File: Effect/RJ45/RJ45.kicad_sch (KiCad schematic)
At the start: 6 parts, among them J1 Conn_01x04_Pin, J2 RJ45, J3 Conn_01x03_Pin

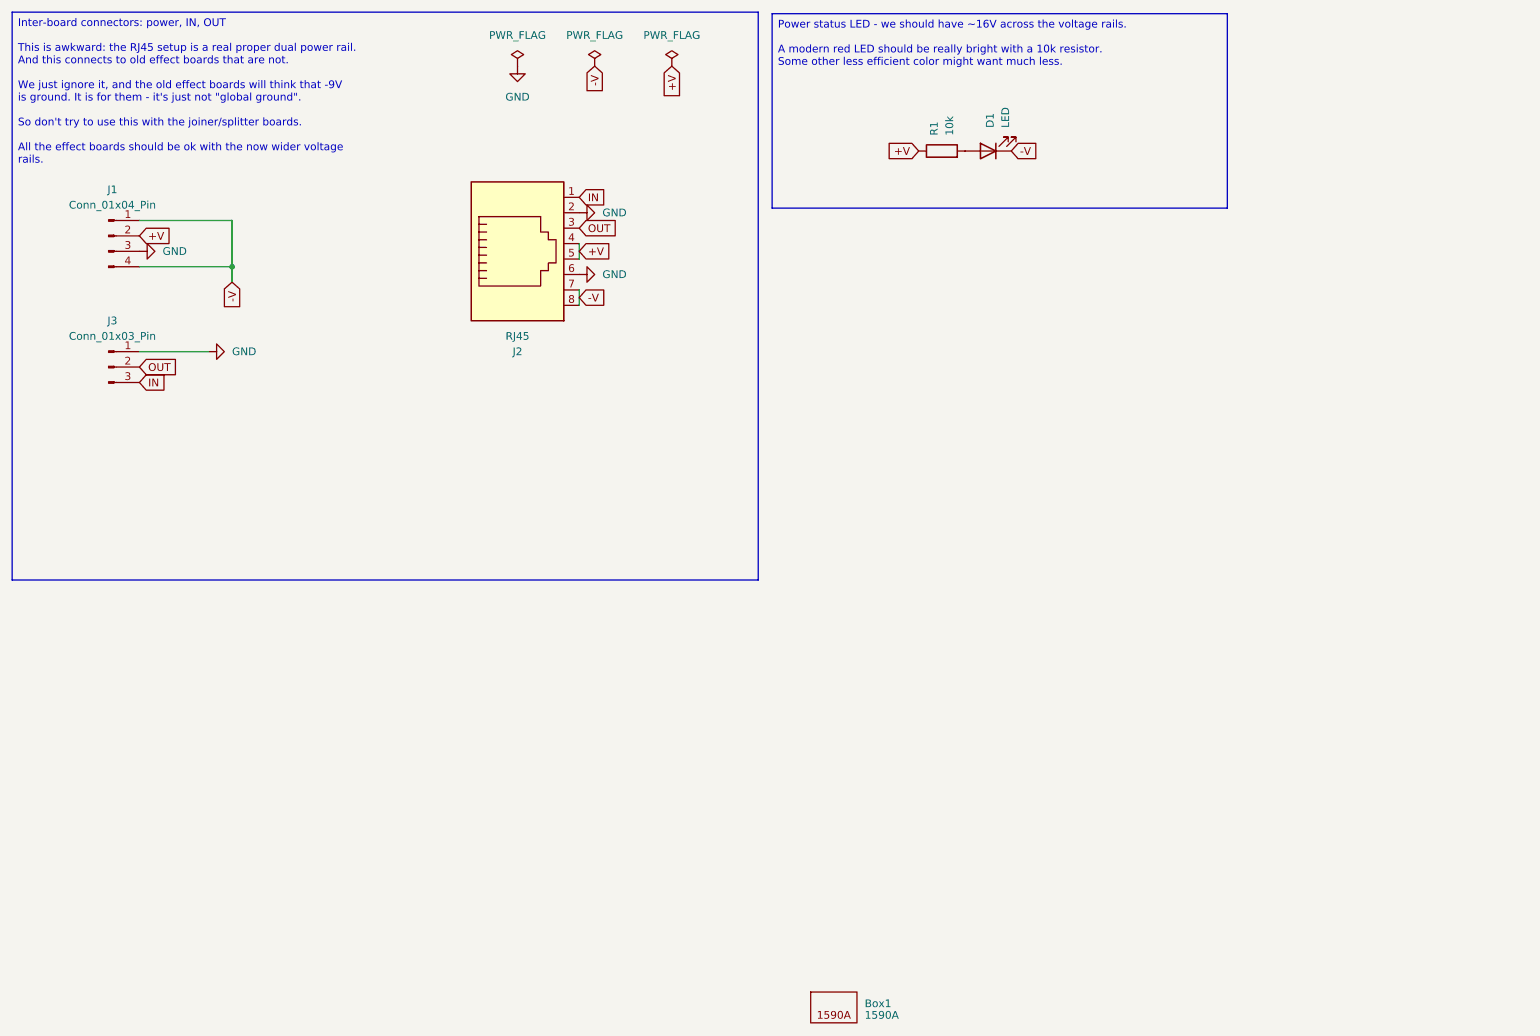
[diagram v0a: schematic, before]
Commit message: Switch to a shielded RJ45 connector for the RJ45 test boards
It turns out that all my ethernet cables I had around look to be plain
unshielded twisted pairs (UTP), and some very preliminary testing shows
that they are very noisy and I'd need to use differential signalling to
make the whole "connect the base and effect with an ethernet cable"
scheme work.

I know, I know, that's technically the right thing to do anyway, but I
really don't think it's an option.  It adds way too much effort at the
effects end, at that point I'm better off just keeping the two together.

Even if some of my recent circuits have been differential (ie that whole
multiplier thing), I don't want to force that on everything.

And yes, the ethernet cable idea might have been a stupid idea and any
first-year EE would probably have told me that.  I'm a SW guy, remember?

But before giving up, let's just try the single-ended model with proper
shielded cables and shielded connectors.  The double-shielded cables are
a thing, with each twisted pair foil-shielded and then the whole cable
having a braided shield.

That would seem to be no worse than a normal 1/4" audio cable, even if
the same cable also carries power.  I'm looking for a few feet, not long
runs.  Knock wood.

And the shielding is part of the CAT8 specs, so this is standard cable
these days and cheap, even if my random box of cables was full of the
old crappy stuff of yesteryear.

So maybe this model is still salvageable with single-ended signaling.
Because I'd love to separate the stomp switch and audio jacks from the
actual effect side.

Signed-off-by: Linus Torvalds <torvalds@linux-foundation.org>
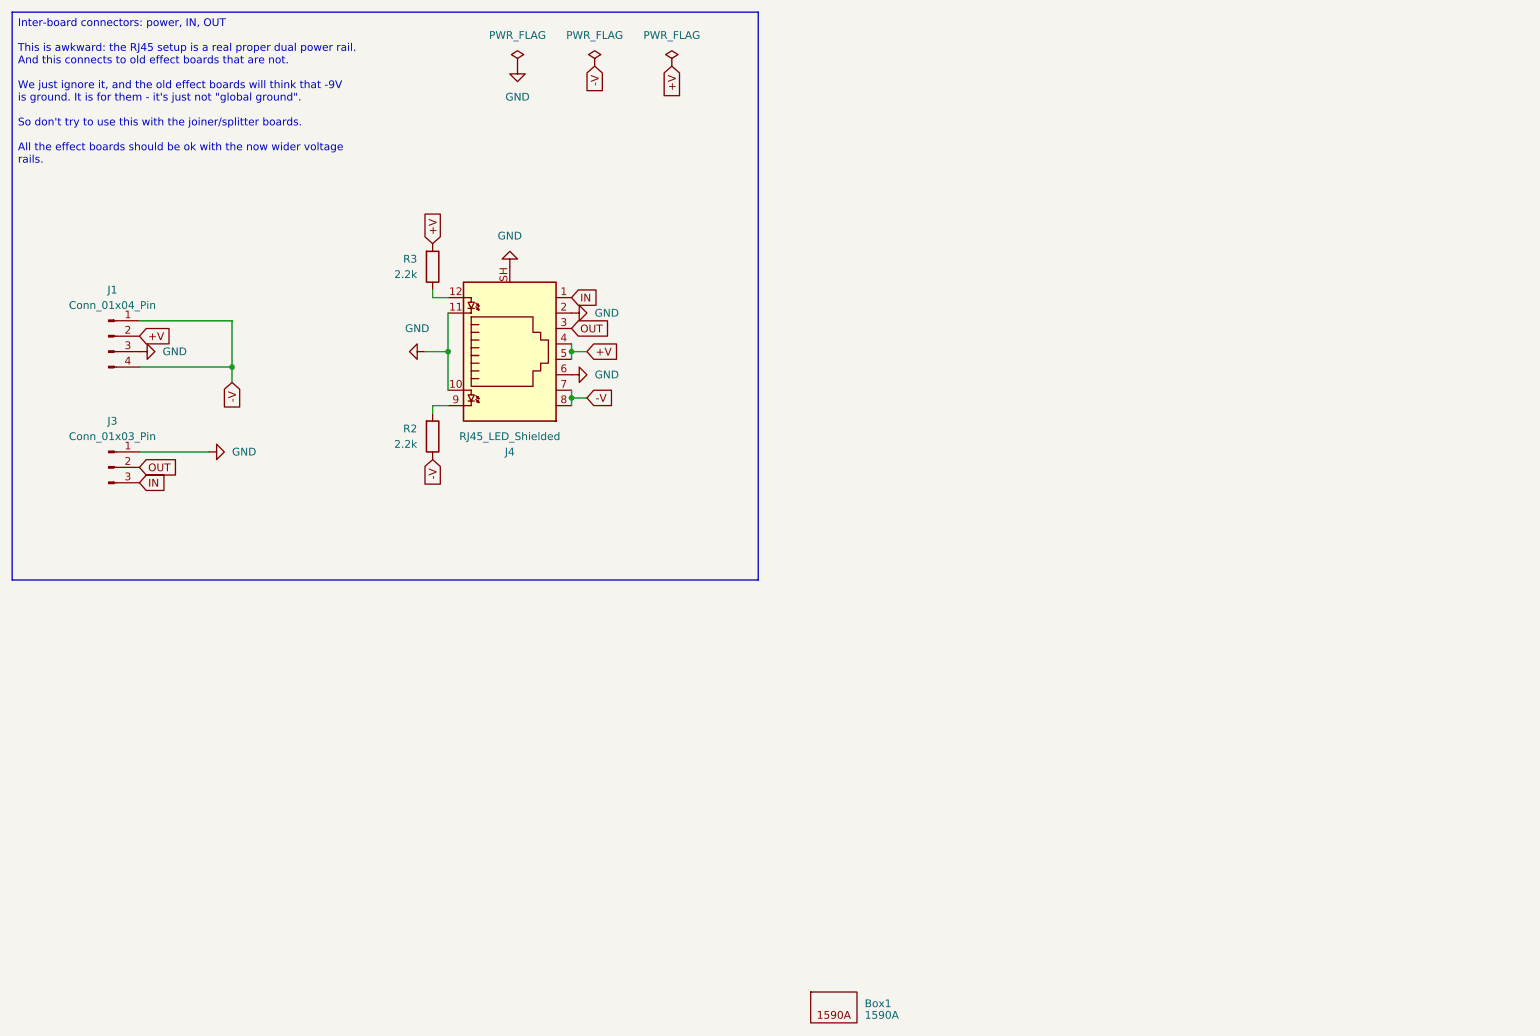
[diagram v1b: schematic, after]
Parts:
- removed D1: LED, Mylib:Würth Reverse Mount LED, symbol Device:LED
- removed J2: RJ45, Connector_RJ:RJ45_OST_PJ012-8P8CX_Vertical, symbol Connector:RJ45
- removed R1: 10k, Resistor_SMD:R_0805_2012Metric, symbol Device:R
- added J4: RJ45_LED_Shielded, Connector_RJ:RJ45_Amphenol_RJHSE538X, symbol Connector:RJ45_LED_Shielded
- added R2, R3: 2.2k, Resistor_SMD:R_0805_2012Metric, symbol Device:R
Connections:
- net +V: now also J4.4, J4.5, R3.2
- net -V: now also J4.7, J4.8, R2.1
- net GND: now also J4.10, J4.11, J4.2, J4.6, J4.SH
- net IN: now also J4.1
- net OUT: now also J4.3
- new net: J4.12, R3.1
- new net: J4.9, R2.2
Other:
- moved on the sheet: J1, J3

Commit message: RJ45: update the "effect conversion" board to be active
... and hopefully make it work right.

The old hacky one was truly just a hack, and was a passive feed-through
of the signals from the RJ45 jack to the old effect board pin headers.

That was hacky mainly because it ignored the whole new world order wrt
voltages (ie the RJ45 cable carries dual voltage rails, the old effect
boards expect the VGND thing).

But it was also hacky because it expected the effects board to just deal
with the fact that the output now went to that RJ45 jack - and that
obviously didn't work very well for the base board, so why would it work
for the effects boards?

So this redoes the conversion board to actually buffer and rebias the
signals, and it basically looks a lot like the old VGND board except it
doesn't have a stomp switch or audio jacks, because all of that is
obviously on the new RJ45 base board.

I put all the components on the front, which in hindsight might have
been a mistake: it means that the joiner and splitter boards won't work
because they won't physically fit any more.  But if we want those in the
new RJ45 regime, I think they probably make more sense as actual new
boards anyway.

Will this work out ok? I still have no idea.  But nothing for it but
try.

Signed-off-by: Linus Torvalds <torvalds@linux-foundation.org>
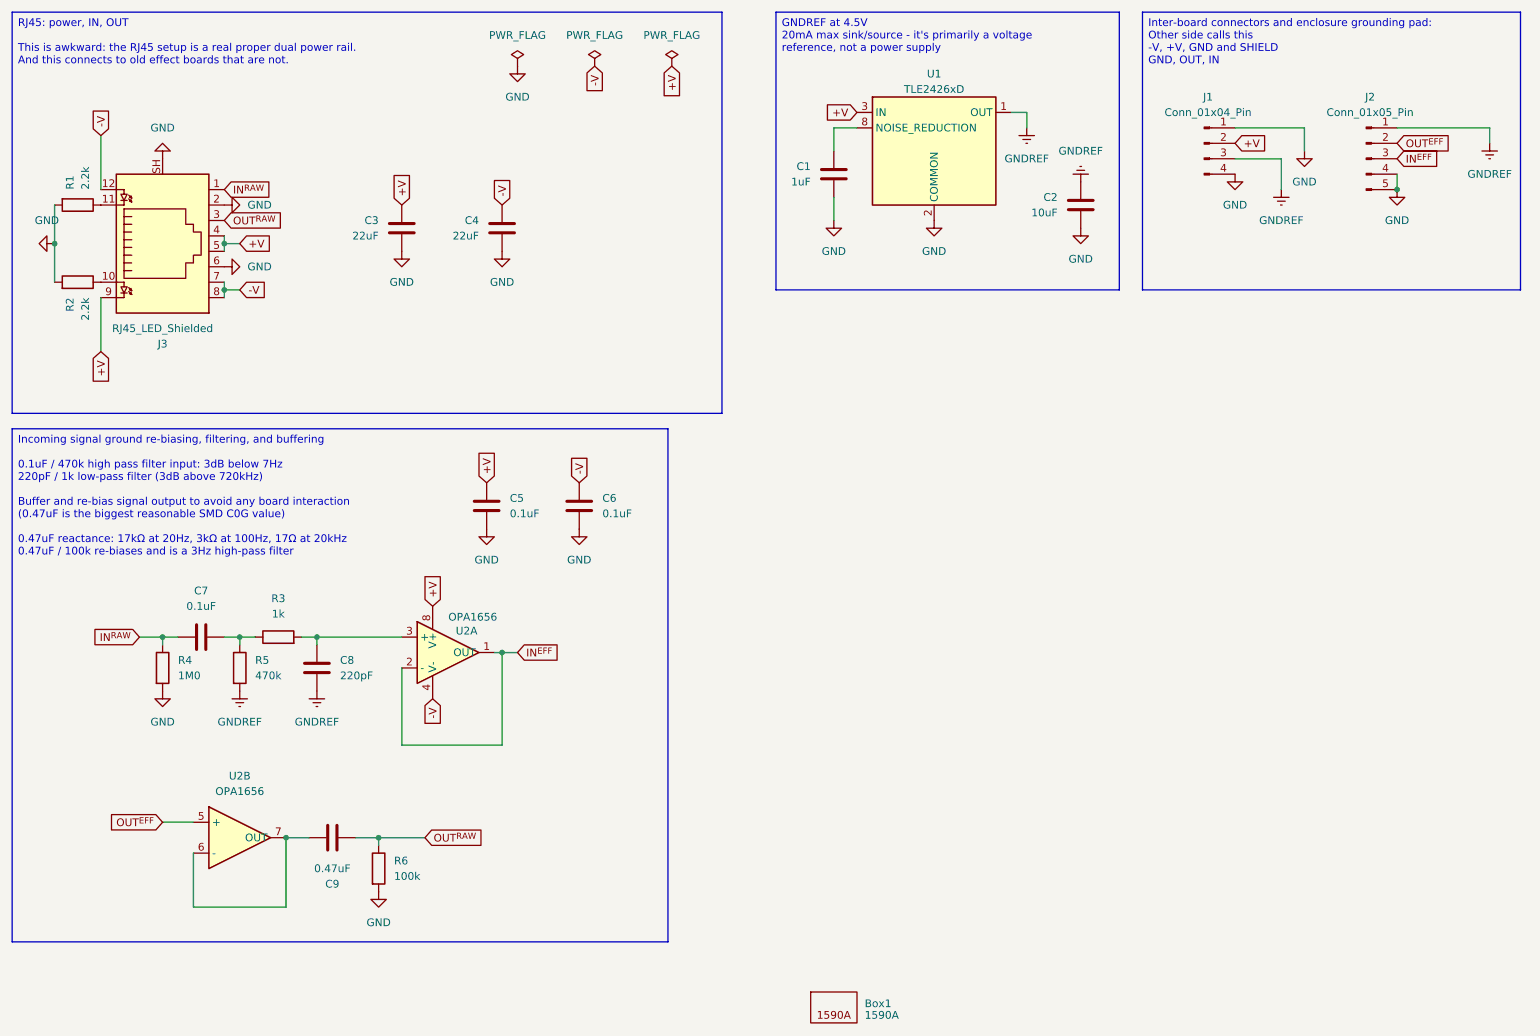
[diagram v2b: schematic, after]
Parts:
- removed J3: Conn_01x03_Pin, Connector_PinSocket_2.54mm:PinSocket_1x03_P2.54mm_Vertical, symbol Connector:Conn_01x03_Pin
- added C1: 1uF, Capacitor_SMD:C_1206_3216Metric_Pad1.33x1.80mm_HandSolder, symbol Device:C
- added C2: 10uF, Capacitor_SMD:C_1206_3216Metric_Pad1.33x1.80mm_HandSolder, symbol Device:C
- added C3, C4: 22uF, Capacitor_SMD:C_1206_3216Metric_Pad1.33x1.80mm_HandSolder, symbol Device:C
- added C5, C6, C7: 0.1uF, Mylib:C_0704_1810Metric, symbol Device:C
- added C8: 220pF, Capacitor_SMD:C_0805_2012Metric_Pad1.18x1.45mm_HandSolder, symbol Device:C
- added C9: 0.47uF, Capacitor_SMD:C_1206_3216Metric_Pad1.33x1.80mm_HandSolder, symbol Device:C
- added J2: Conn_01x05_Pin, Connector_PinSocket_2.54mm:PinSocket_1x05_P2.54mm_Vertical, symbol Connector:Conn_01x05_Pin
- added R3: 1k, Resistor_SMD:R_0805_2012Metric_Pad1.20x1.40mm_HandSolder, symbol Device:R
- added R4: 1M0, Resistor_SMD:R_0805_2012Metric_Pad1.20x1.40mm_HandSolder, symbol Device:R
- added R5: 470k, Resistor_SMD:R_0805_2012Metric_Pad1.20x1.40mm_HandSolder, symbol Device:R
- added R6: 100k, Resistor_SMD:R_0805_2012Metric_Pad1.20x1.40mm_HandSolder, symbol Device:R
- added U1: TLE2426xD, Package_SO:SOIC-8_3.9x4.9mm_P1.27mm, symbol Reference_Voltage:TLE2426xD
- added U2: OPA1656, Package_SO:SOIC-8_3.9x4.9mm_P1.27mm, symbol Mylib:OPA1656
- renumbered J4 to J3, R3 to R1
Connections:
- net +V: now also J3.9, C3.1, C5.1, U1.3 (IN), U2.8 (V+); no longer R1.2
- net -V: now also J3.12, C4.1, C6.1, U2.4 (V-); no longer J1.1 (Pin_1), J1.4 (Pin_4), R2.1
- net GND: now also J1.1 (Pin_1), J1.4 (Pin_4), R1.2, R2.2, C1.2, C2.2, C3.2, C4.2, C5.2, C6.2, J2.4 (Pin_4), J2.5 (Pin_5), R4.2, R6.2, U1.2 (COMMON); no longer J1.3 (Pin_3), J3.10, J3.11
- net at R1.1: now also J3.11; no longer J3.12
- net IN renamed IN^{RAW}
- net IN^{RAW}: now also C7.1, R4.1
- net OUT renamed OUT^{RAW}
- net OUT^{RAW}: now also C9.1, R6.1
- new net: C9.2, U2.6 (-), U2.7 (OUT)
- new net: C7.2, R3.1, R5.1
- new net: C8.1, R3.2, U2.3 (+)
- new net: C1.1, U1.8 (NOISE_REDUCTION)
- new net: J3.10, R2.1
- new net GNDREF: C2.1, C8.2, J1.3 (Pin_3), J2.1 (Pin_1), R5.2, U1.1 (OUT)
- new net IN^{EFF}: J2.3 (Pin_3), U2.1 (OUT), U2.2 (-)
- new net OUT^{EFF}: J2.2 (Pin_2), U2.5 (+)
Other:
- moved on the sheet: J3, R1, R2

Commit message: Update the RJ45 boards
So I'm doing two different cable versions in parallel to see which I
like better.  The "passive base board" version uses USB-C connectors and
really doesn't do anything at all but convert the power, stomp switch
and audio connectors to one single cable.  So the effects board is
supposed to do everything that is actually signal-related, including
generating its own reference voltages etc.

In contrast, the RJ45 board is "active", and also generates a negative
power rail.  That doesn't help the existing effects boards, but it means
that any boards actively designed for this have all the voltages
(assuming +-9V and GND works for them), and don't need to rebias signals
etc.

Do I know which board - if any - I'm actually going to develop further?
No.  They may both be garbage.

Signed-off-by: Linus Torvalds <torvalds@linux-foundation.org>
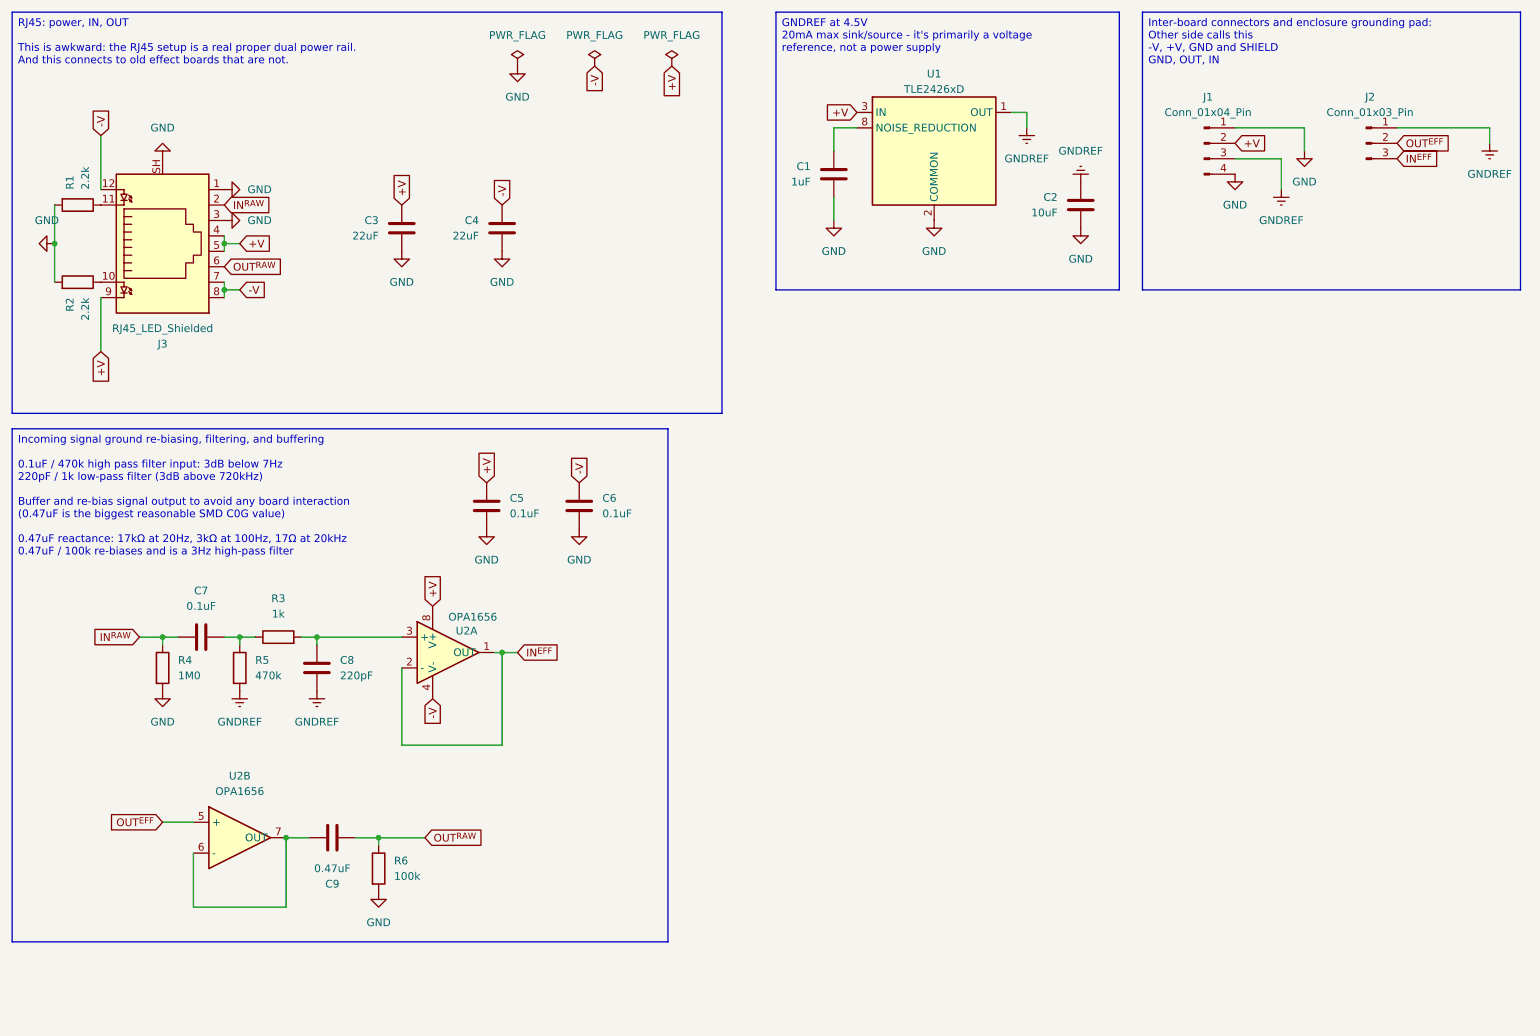
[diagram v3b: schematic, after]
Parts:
- removed Box1: 1590A, Mylib:1590A, symbol Mylib:Enclosure_1590A
- removed J2: Conn_01x05_Pin, Connector_PinSocket_2.54mm:PinSocket_1x05_P2.54mm_Vertical, symbol Connector:Conn_01x05_Pin
- added J2: Conn_01x03_Pin, Connector_PinSocket_2.54mm:PinSocket_1x03_P2.54mm_Vertical, symbol Connector:Conn_01x03_Pin
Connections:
- net GND: now also J3.1, J3.3; no longer J3.2, J3.6
- net GNDREF: now also J2.1 (Pin_1)
- net IN^{EFF}: now also J2.3 (Pin_3)
- net IN^{RAW}: now also J3.2; no longer J3.1
- net OUT^{EFF}: now also J2.2 (Pin_2)
- net OUT^{RAW}: now also J3.6; no longer J3.3
